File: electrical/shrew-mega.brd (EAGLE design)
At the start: 18 x 15 mm, 21 parts, among them U1 DRV8244SQRYJRQ1, U2 DRV8244SQRYJRQ1, X1 PIN-1X-BIG, X2 PIN-1X-BIG, X3 PIN-1X-BIG, X4 PIN-1X-BIG, X5 PIN-1X-BIG, X6 PIN-1X-BIG

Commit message: more mfg files
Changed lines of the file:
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@@
 <layer number="19" name="Unrouted" color="6" fill="1" visible="yes" active="yes"/>
 <layer number="20" name="Dimension" color="15" fill="1" visible="yes" active="yes"/>
-<layer number="21" name="tPlace" color="7" fill="1" visible="no" active="yes"/>
-<layer number="22" name="bPlace" color="7" fill="1" visible="no" active="yes"/>
+<layer number="21" name="tPlace" color="7" fill="1" visible="yes" active="yes"/>
+<layer number="22" name="bPlace" color="7" fill="1" visible="yes" active="yes"/>
 <layer number="23" name="tOrigins" color="15" fill="1" visible="no" active="yes"/>
 <layer number="24" name="bOrigins" color="15" fill="1" visible="no" active="yes"/>
@@
 <layer number="39" name="tKeepout" color="4" fill="11" visible="no" active="yes"/>
 <layer number="40" name="bKeepout" color="1" fill="11" visible="no" active="yes"/>
-<layer number="41" name="tRestrict" color="4" fill="10" visible="yes" active="yes"/>
-<layer number="42" name="bRestrict" color="1" fill="10" visible="yes" active="yes"/>
+<layer number="41" name="tRestrict" color="4" fill="10" visible="no" active="yes"/>
+<layer number="42" name="bRestrict" color="1" fill="10" visible="no" active="yes"/>
 <layer number="43" name="vRestrict" color="2" fill="10" visible="no" active="yes"/>
 <layer number="44" name="Drills" color="7" fill="1" visible="no" active="yes"/>
@@
 <wire x1="18" y1="15" x2="0" y2="15" width="0" layer="20"/>
 <wire x1="0" y1="15" x2="0" y2="0" width="0" layer="20"/>
-<rectangle x1="1.5" y1="3.3" x2="5.7" y2="4.8" layer="30"/>
 <wire x1="2.14" y1="7.88" x2="2.14" y2="4.48" width="0" layer="42"/>
 <wire x1="2.14" y1="4.48" x2="2.13" y2="4.48" width="0" layer="42"/>
@@
 <polygon width="0" layer="29" spacing="0.254">
 <vertex x="3.6" y="7.6"/>
-<vertex x="1.5" y="7.6"/>
-<vertex x="1.5" y="2.7"/>
+<vertex x="1.6" y="7.6"/>
+<vertex x="1.6" y="2.7"/>
 <vertex x="3" y="2.7"/>
 <vertex x="3" y="6.3"/>
@@
 <polygon width="0" layer="29" spacing="0.254">
 <vertex x="7" y="7.6"/>
-<vertex x="8.3" y="7.6"/>
-<vertex x="8.3" y="6.6"/>
-<vertex x="8.3" y="2.9"/>
+<vertex x="8.5" y="7.6"/>
+<vertex x="8.5" y="2.9"/>
 <vertex x="6.3" y="2.9"/>
 <vertex x="6.3" y="3.9"/>
-<vertex x="6.5" y="3.9"/>
 <vertex x="7.4" y="3.9"/>
 <vertex x="7.4" y="6.3"/>
@@
 <vertex x="11.8" y="3.8"/>
 <vertex x="11.8" y="2.8"/>
-<vertex x="9.7" y="2.8"/>
-<vertex x="9.7" y="7.6"/>
+<vertex x="9.5" y="2.8"/>
+<vertex x="9.5" y="7.6"/>
 </polygon>
 <polygon width="0" layer="29" spacing="0.254">
@@
 <vertex x="14.5" y="6.3"/>
 </polygon>
-<wire x1="0.2" y1="14.4" x2="18" y2="14.4" width="0" layer="41"/>
+<wire x1="0.1" y1="14" x2="17.9" y2="14" width="0" layer="41"/>
 <wire x1="18" y1="14.4" x2="0.2" y2="14.4" width="0" layer="42"/>
 </plain>
@@
 <wire x1="10.2" y1="11.2" x2="10.2" y2="10.5" width="0.6" layer="16"/>
 <via x="9" y="3" extent="1-16" drill="0.3" shape="octagon"/>
-<wire x1="9" y1="3" x2="9" y2="7.2" width="0.6" layer="1"/>
-<via x="9" y="7.2" extent="1-16" drill="0.3" shape="octagon"/>
-<wire x1="9" y1="7.2" x2="9" y2="10.499" width="1" layer="16"/>
+<wire x1="9" y1="3" x2="9" y2="7.4" width="0.6" layer="1"/>
+<via x="9" y="7.4" extent="1-16" drill="0.3" shape="octagon"/>
+<wire x1="9" y1="7.4" x2="9" y2="10.499" width="1" layer="16"/>
 <wire x1="9" y1="4.3012" x2="9" y2="3" width="0.6" layer="16"/>
 <wire x1="13" y1="14" x2="13.52" y2="13.48" width="0.6" layer="16"/>
 <wire x1="13.52" y1="13.48" x2="13.52" y2="12.3" width="0.6" layer="16"/>
-<wire x1="13.52" y1="12.3" x2="13.52" y2="10.1" width="0.6" layer="16"/>
-<wire x1="13.52" y1="10.1" x2="10.2" y2="10.1" width="0.6" layer="16"/>
+<wire x1="13.52" y1="12.3" x2="13.52" y2="10.78" width="0.6" layer="16"/>
+<wire x1="13.52" y1="10.78" x2="12.84" y2="10.1" width="0.6" layer="16"/>
+<wire x1="12.84" y1="10.1" x2="10.2" y2="10.1" width="0.6" layer="16"/>
 <wire x1="10.2" y1="10.1" x2="10.2" y2="10.5" width="0.6" layer="16"/>
 <wire x1="3.2" y1="10.7" x2="3.5" y2="11" width="0.1524" layer="1"/>
@@
 <wire x1="6.1" y1="11" x2="6.3" y2="11.2" width="0.1524" layer="1"/>
 <via x="6.3" y="11.2" extent="1-16" drill="0.3" shape="octagon"/>
-<wire x1="6.3" y1="11.2" x2="8.299" y2="11.2" width="0.1524" layer="16"/>
+<wire x1="6.3" y1="11.2" x2="8.299" y2="11.2" width="0.3048" layer="16"/>
 <wire x1="8.299" y1="11.2" x2="9" y2="10.499" width="0.1524" layer="16"/>
 </signal>

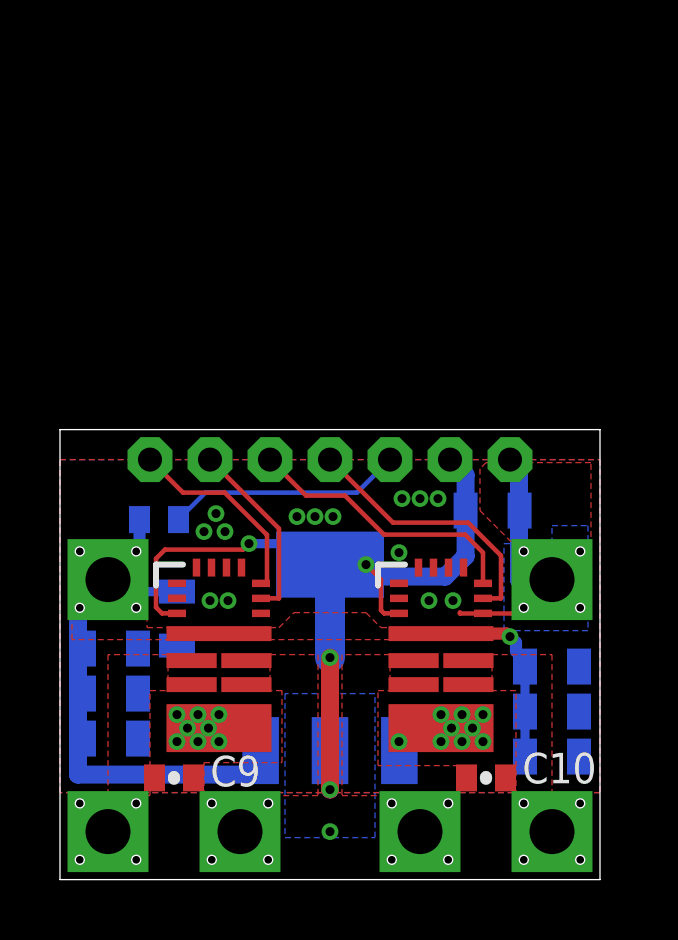
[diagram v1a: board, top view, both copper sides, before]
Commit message: changed v-reg on the mega variant to be more avail
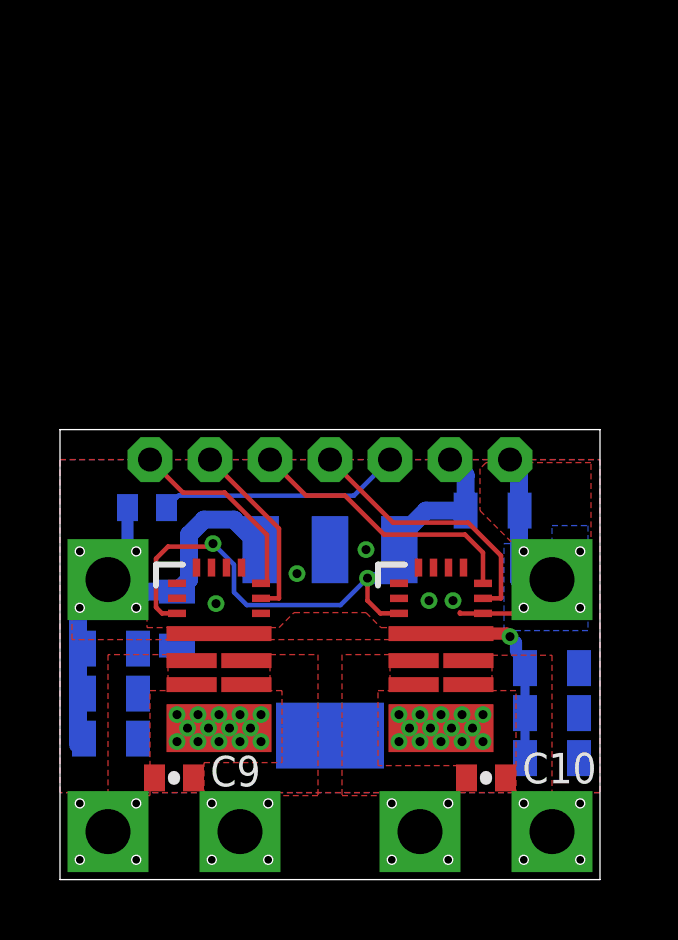
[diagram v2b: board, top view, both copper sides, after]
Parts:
- moved R1 0.57 mm to (2.90, 12.4)
- moved IC1 0.50 mm to (9.00, 7.90), turned to 180 degrees
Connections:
- net +24V: now also IC1.1; no longer IC1.3
- net 3.3V: now also IC1.3; no longer IC1.2, IC1.4
- net GND: now also IC1.2, IC1.4; no longer IC1.1
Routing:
- net 3.3V: track 29.8 -> 20.3 mm, vias 4 -> 2
- net +24V: track 27.0 -> 24.3 mm
- net GND: vias 32 -> 33

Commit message: schematic stitcher
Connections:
- net N$10 renamed MOTOR3
- net N$4 renamed MOTOR2
- net N$5 renamed MOTOR1
- net N$7 renamed V-ADC
- net N$8 renamed MOTOR4
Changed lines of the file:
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@@
 <wire x1="2.25" y1="10.65" x2="1.6" y2="10" width="0.4064" layer="16"/>
 </signal>
-<signal name="N$4">
+<signal name="MOTOR2">
 <contactref element="X1" pad="1"/>
 <contactref element="C9" pad="2"/>
@@
 </polygon>
 </signal>
-<signal name="N$5">
+<signal name="MOTOR1">
 <contactref element="X2" pad="1"/>
 <contactref element="C9" pad="1"/>
@@
 </polygon>
 </signal>
-<signal name="N$8">
+<signal name="MOTOR4">
 <contactref element="X3" pad="1"/>
 <contactref element="C10" pad="2"/>
@@
 </polygon>
 </signal>
-<signal name="N$10">
+<signal name="MOTOR3">
 <contactref element="X4" pad="1"/>
 <contactref element="C10" pad="1"/>
@@
 <wire x1="8.2" y1="12.8" x2="7" y2="14" width="0.1524" layer="1"/>
 </signal>
-<signal name="N$7">
+<signal name="V-ADC">
 <contactref element="JP1" pad="3"/>
 <contactref element="R1" pad="1"/>

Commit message: added power input silk
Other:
- board text added: "G"
- board text added: "V"
- board text added: "V+"
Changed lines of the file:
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@@
 <wire x1="0.1" y1="14" x2="17.9" y2="14" width="0" layer="41"/>
 <wire x1="18" y1="14.4" x2="0.2" y2="14.4" width="0" layer="42"/>
+<text x="16.5" y="12.1" size="1" layer="21" font="vector" align="center">G</text>
+<text x="17.1" y="12.1" size="1" layer="22" font="vector" rot="MR0" align="center">G</text>
+<text x="1.6" y="12.2" size="1" layer="21" font="vector" align="center">V+</text>
+<text x="0.7" y="12.2" size="1" layer="22" font="vector" rot="MR0" align="center">V</text>
 </plain>
 <attributes>

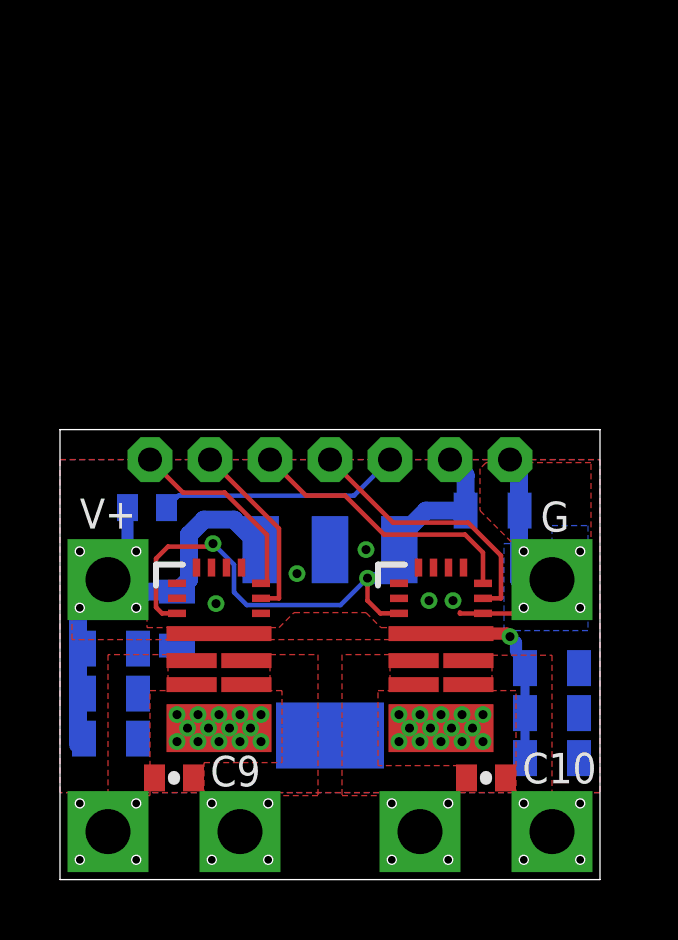
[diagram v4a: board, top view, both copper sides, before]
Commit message: initial work on integrated versions
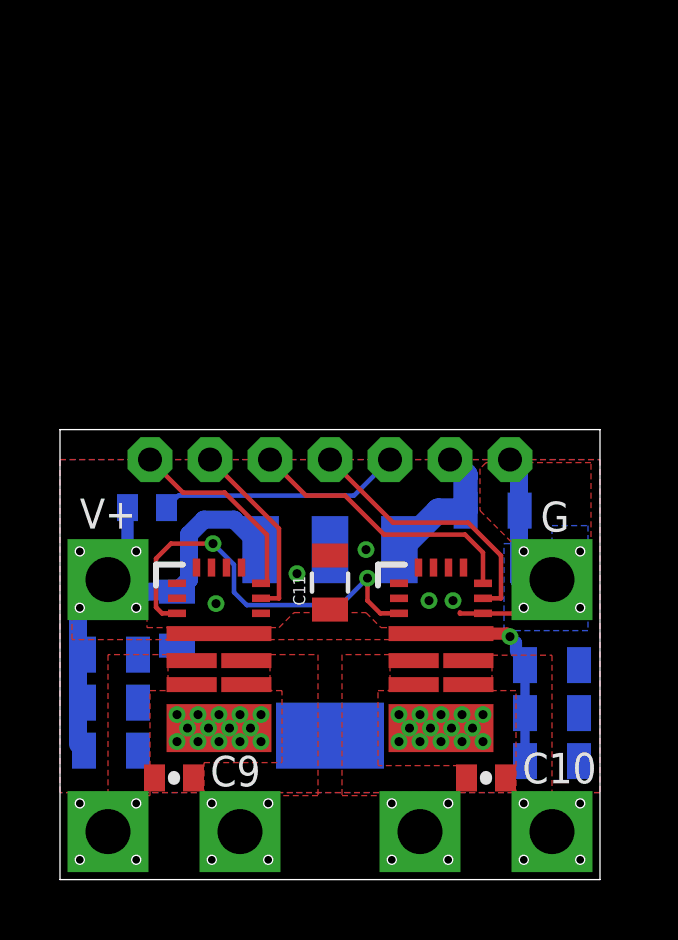
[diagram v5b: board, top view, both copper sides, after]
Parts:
- added C11: (no value), shrew-common:0805
- moved C1 0.40 mm to (1.70, 4.30)
- moved C2 0.30 mm to (1.70, 5.90)
- moved C3 0.20 mm to (1.70, 7.50)
- moved C5 0.10 mm to (16.4, 7.15)
- moved C7 0.10 mm to (16.4, 3.95)
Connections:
- new net SLEEP: U1.3, U2.3
- net +24V: now also C11.1
- net 3.3V: no longer U1.3, U2.3
- net GND: now also C11.2
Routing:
- net 3.3V: track 20.3 -> 4.66 mm, vias 2 -> 0
- net SLEEP: track 0.00 -> 13.4 mm, vias 0 -> 2
- net +24V: track 24.3 -> 24.9 mm
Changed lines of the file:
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@@
 <layer number="97" name="Info" color="7" fill="1" visible="no" active="no"/>
 <layer number="98" name="Guide" color="6" fill="1" visible="no" active="no"/>
+<layer number="99" name="SpiceOrder" color="5" fill="1" visible="no" active="no"/>
 <layer number="100" name="Muster" color="7" fill="1" visible="no" active="no"/>
 <layer number="101" name="Patch_Top" color="12" fill="4" visible="no" active="yes"/>
@@
 <element name="X5" library="shrew-core" package="PAD-1X-BIG" value="PIN-1X-BIG" x="1.6" y="10" smashed="yes"/>
 <element name="X6" library="shrew-core" package="PAD-1X-BIG" value="PIN-1X-BIG" x="16.4" y="10" smashed="yes"/>
-<element name="C1" library="shrew-common" package="0805" value="" x="1.7" y="4.7" smashed="yes" rot="MR180">
-<attribute name="NAME" x="3.238" y="5.1745" size="1.016" layer="26" font="vector" rot="MR180"/>
-<attribute name="VALUE" x="0.684" y="6.097" size="0.4064" layer="28" rot="MR180"/>
-</element>
-<element name="C2" library="shrew-common" package="0805" value="" x="1.7" y="6.2" smashed="yes" rot="MR180">
-<attribute name="NAME" x="3.238" y="6.6745" size="1.016" layer="26" font="vector" rot="MR180"/>
-<attribute name="VALUE" x="0.684" y="7.597" size="0.4064" layer="28" rot="MR180"/>
-</element>
-<element name="C3" library="shrew-common" package="0805" value="" x="1.7" y="7.7" smashed="yes" rot="MR180">
-<attribute name="NAME" x="3.138" y="8.1745" size="1.016" layer="26" font="vector" rot="MR180"/>
-<attribute name="VALUE" x="0.684" y="9.097" size="0.4064" layer="28" rot="MR180"/>
+<element name="C1" library="shrew-common" package="0805" value="" x="1.7" y="4.3" smashed="yes" rot="MR180">
+<attribute name="NAME" x="3.238" y="4.7745" size="1.016" layer="26" font="vector" rot="MR180"/>
+<attribute name="VALUE" x="0.684" y="5.697" size="0.4064" layer="28" rot="MR180"/>
+</element>
+<element name="C2" library="shrew-common" package="0805" value="" x="1.7" y="5.9" smashed="yes" rot="MR180">
+<attribute name="NAME" x="3.238" y="6.3745" size="1.016" layer="26" font="vector" rot="MR180"/>
+<attribute name="VALUE" x="0.684" y="7.297" size="0.4064" layer="28" rot="MR180"/>
+</element>
+<element name="C3" library="shrew-common" package="0805" value="" x="1.7" y="7.5" smashed="yes" rot="MR180">
+<attribute name="NAME" x="3.138" y="7.9745" size="1.016" layer="26" font="vector" rot="MR180"/>
+<attribute name="VALUE" x="0.684" y="8.897" size="0.4064" layer="28" rot="MR180"/>
 </element>
 <element name="C4" library="shrew-common" package="0805" value="" x="3.9" y="8.7" smashed="yes" rot="MR270">
@@
 <attribute name="NAME" x="9.4234" y="6.865" size="1.016" layer="27" font="vector" ratio="6" rot="SR0"/>
 </element>
-<element name="C5" library="shrew-common" package="0805" value="" x="16.4" y="7.05" smashed="yes" rot="MR180">
-<attribute name="NAME" x="15.638" y="6.2245" size="1.016" layer="26" font="vector" rot="MR180"/>
-<attribute name="VALUE" x="15.384" y="8.447" size="0.4064" layer="28" rot="MR180"/>
+<element name="C5" library="shrew-common" package="0805" value="" x="16.4" y="7.15" smashed="yes" rot="MR180">
+<attribute name="NAME" x="15.638" y="6.3245" size="1.016" layer="26" font="vector" rot="MR180"/>
+<attribute name="VALUE" x="15.384" y="8.547" size="0.4064" layer="28" rot="MR180"/>
 </element>
 <element name="C6" library="shrew-common" package="0805" value="" x="16.4" y="5.55" smashed="yes" rot="MR180">
@@
 <attribute name="VALUE" x="15.384" y="6.947" size="0.4064" layer="28" rot="MR180"/>
 </element>
-<element name="C7" library="shrew-common" package="0805" value="" x="16.4" y="4.05" smashed="yes" rot="MR180">
-<attribute name="NAME" x="15.638" y="3.2245" size="1.016" layer="26" font="vector" rot="MR180"/>
-<attribute name="VALUE" x="15.384" y="5.447" size="0.4064" layer="28" rot="MR180"/>
+<element name="C7" library="shrew-common" package="0805" value="" x="16.4" y="3.95" smashed="yes" rot="MR180">
+<attribute name="NAME" x="15.638" y="3.1245" size="1.016" layer="26" font="vector" rot="MR180"/>
+<attribute name="VALUE" x="15.384" y="5.347" size="0.4064" layer="28" rot="MR180"/>
 </element>
 <element name="IC1" library="shrew-common" package="SOT223" value="" x="9" y="7.9" rot="MR180"/>
+<element name="C11" library="shrew-common" package="0805" value="" x="9" y="9.9" rot="R90"/>
 </elements>
 <signals>
@@
 <via x="7.9" y="10.2" extent="1-16" drill="0.3" shape="square"/>
 <via x="10.2" y="11" extent="1-16" drill="0.3" shape="square"/>
+<contactref element="C11" pad="2"/>
 </signal>
 <signal name="VDD_SDIO">
 </signal>
-<signal name="3.3V">
-<contactref element="JP1" pad="2"/>
-<contactref element="C8" pad="1"/>
-<contactref element="U1" pad="3"/>
-<contactref element="U2" pad="3"/>
-<wire x1="3.9" y1="8.875" x2="3.40155625" y2="8.875" width="0.1524" layer="1"/>
+<signal name="SLEEP">
 <wire x1="3.40155625" y1="8.875" x2="3.2" y2="9.07655625" width="0.1524" layer="1"/>
 <wire x1="3.2" y1="9.07655625" x2="3.2" y2="10.7" width="0.1524" layer="1"/>
 <via x="10.25" y="10.05" extent="1-16" drill="0.3" shape="octagon"/>
-<wire x1="13" y1="14" x2="13.52" y2="13.48" width="0.6" layer="16"/>
-<wire x1="13.52" y1="13.48" x2="13.52" y2="12.3" width="0.6" layer="16"/>
-<wire x1="3.2" y1="10.7" x2="3.6" y2="11.1" width="0.1524" layer="1"/>
-<wire x1="3.6" y1="11.1" x2="5" y2="11.1" width="0.1524" layer="1"/>
-<wire x1="5" y1="11.1" x2="5.1" y2="11.2" width="0.1524" layer="1"/>
+<wire x1="3.2" y1="10.7" x2="3.7" y2="11.2" width="0.1524" layer="1"/>
 <via x="5.1" y="11.2" extent="1-16" drill="0.3" shape="octagon"/>
-<contactref element="IC1" pad="3"/>
-<wire x1="11.3" y1="8.875" x2="10.675" y2="8.875" width="0.1524" layer="1"/>
 <wire x1="10.675" y1="8.875" x2="10.25" y2="9.3" width="0.1524" layer="1"/>
 <wire x1="10.25" y1="9.3" x2="10.25" y2="10.05" width="0.1524" layer="1"/>
@@
 <wire x1="6.2272" y1="9.15" x2="9.35" y2="9.15" width="0.1524" layer="16"/>
 <wire x1="9.35" y1="9.15" x2="10.25" y2="10.05" width="0.1524" layer="16"/>
-<wire x1="10.25" y1="10.05" x2="11.3114" y2="10.05" width="0.4064" layer="16"/>
-<wire x1="11.3114" y1="10.05" x2="11.3114" y2="10.9988" width="0.4064" layer="16"/>
-<wire x1="13.52" y1="12.3" x2="12.2" y2="12.3" width="0.6" layer="16"/>
-<wire x1="12.2" y1="12.3" x2="11.3114" y2="11.4114" width="0.6" layer="16"/>
-<wire x1="11.3114" y1="11.4114" x2="11.3114" y2="10.9988" width="0.6" layer="16"/>
+<contactref element="U1" pad="3"/>
+<contactref element="U2" pad="3"/>
+<wire x1="3.9" y1="8.875" x2="3.40155625" y2="8.875" width="0.1524" layer="1"/>
+<wire x1="11.3" y1="8.875" x2="10.675" y2="8.875" width="0.1524" layer="1"/>
+<wire x1="3.7" y1="11.2" x2="5.1" y2="11.2" width="0.1524" layer="1"/>
 </signal>
 <signal name="+24V">
@@
 <wire x1="15.2" y1="7.9" x2="15.2" y2="7.6" width="0.4064" layer="16"/>
 <wire x1="15.2" y1="7.6" x2="15.5" y2="7.3" width="0.3048" layer="16"/>
-<wire x1="15.5" y1="7.05" x2="15.5" y2="5.55" width="0.3048" layer="16"/>
-<wire x1="15.5" y1="5.55" x2="15.5" y2="4.05" width="0.3048" layer="16"/>
-<wire x1="15.5" y1="7.3" x2="15.5" y2="7.05" width="0.3048" layer="16"/>
-<wire x1="0.8" y1="4.7" x2="0.6" y2="4.7" width="0.3048" layer="16"/>
+<wire x1="15.5" y1="7.15" x2="15.5" y2="5.55" width="0.3048" layer="16"/>
+<wire x1="15.5" y1="5.55" x2="15.5" y2="3.95" width="0.3048" layer="16"/>
+<wire x1="15.5" y1="7.3" x2="15.5" y2="7.15" width="0.3048" layer="16"/>
+<wire x1="0.8" y1="4.3" x2="0.6" y2="4.7" width="0.3048" layer="16"/>
 <wire x1="0.6" y1="4.7" x2="0.6" y2="4.5" width="0.3048" layer="16"/>
-<wire x1="0.8" y1="6.2" x2="0.6" y2="6.2" width="0.3048" layer="16"/>
+<wire x1="0.8" y1="5.9" x2="0.6" y2="6.2" width="0.3048" layer="16"/>
 <wire x1="0.6" y1="6.2" x2="0.6" y2="5.8" width="0.3048" layer="16"/>
-<wire x1="0.8" y1="7.7" x2="0.6" y2="7.7" width="0.3048" layer="16"/>
+<wire x1="0.8" y1="7.5" x2="0.6" y2="7.7" width="0.3048" layer="16"/>
 <wire x1="0.6" y1="7.7" x2="0.6" y2="8" width="0.3048" layer="16"/>
 <contactref element="IC1" pad="1"/>
@@
 <wire x1="2.25" y1="12.4" x2="2.25" y2="10.65" width="0.4064" layer="16"/>
 <wire x1="2.25" y1="10.65" x2="1.6" y2="10" width="0.4064" layer="16"/>
+<contactref element="C11" pad="1"/>
 </signal>
 <signal name="MOTOR2">
@@
 <wire x1="3.95" y1="12.8" x2="3.55" y2="12.4" width="0.1524" layer="16"/>
 </signal>
+<signal name="3.3V">
+<contactref element="JP1" pad="2"/>
+<contactref element="IC1" pad="3"/>
+<contactref element="C8" pad="1"/>
+<wire x1="11.3114" y1="10.9988" x2="12.6126" y2="12.3" width="0.8128" layer="16"/>
+<wire x1="12.6126" y1="12.3" x2="13.52" y2="12.3" width="0.8128" layer="16"/>
+<wire x1="13" y1="14" x2="13.52" y2="13.48" width="0.8128" layer="16"/>
+<wire x1="13.52" y1="13.48" x2="13.52" y2="12.3" width="0.8128" layer="16"/>
+</signal>
 </signals>
